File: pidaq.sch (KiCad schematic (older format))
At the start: 7 parts, among them J5 Conn_01x03_Male, J6 Conn_01x08_Female, U3 SN74LV1T34DCKR

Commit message: completed design 2.0
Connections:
- net GND: now also J6.5 (Pin_5); no longer J6.4 (Pin_4)
- net IRQ: now also J6.4 (Pin_4); no longer J6.3 (Pin_3)
- net MISO_SAFE: now also J6.8 (Pin_8); no longer J6.7 (Pin_7)
- net MOSI: now also J6.6 (Pin_6); no longer J6.5 (Pin_5)
- net SCLK: now also J6.7 (Pin_7); no longer J6.6 (Pin_6)
- net ~RST: now also J6.3 (Pin_3); no longer J6.2 (Pin_2)
- net ~SEN: now also J6.1 (Pin_1); no longer J6.8 (Pin_8)
- net ~TC: now also J6.2 (Pin_2); no longer J6.1 (Pin_1)
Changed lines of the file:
@@
 	1    0    0    -1
 $EndComp
-Text GLabel 9150 2900 0    50   Input ~ 0
+Text GLabel 9150 2200 0    50   Input ~ 0
 ~SEN
-Text GLabel 9150 2400 0    50   Input ~ 0
+Text GLabel 9150 2500 0    50   Input ~ 0
 IRQ
-Text GLabel 9150 2500 0    50   Input ~ 0
+Text GLabel 9150 2600 0    50   Input ~ 0
 GND
+Text GLabel 9150 2800 0    50   Input ~ 0
+SCLK
 Text GLabel 9150 2700 0    50   Input ~ 0
-SCLK
-Text GLabel 9150 2600 0    50   Input ~ 0
 MOSI
 Text GLabel 6750 2850 0    50   Input ~ 0
@@
 GND
 Wire Wire Line
-	9150 2800 8250 2800
-Wire Wire Line
 	8250 2800 8250 2850
 Wire Notes Line
@@
 Text Label 8350 2800 0    50   ~ 0
 MISO_SAFE
-Text GLabel 9150 2200 0    50   Input ~ 0
+Text GLabel 9150 2300 0    50   Input ~ 0
 ~TC
 $Comp
@@
 Text GLabel 4600 4850 2    50   Input ~ 0
 ~RST
-Text GLabel 9150 2300 0    50   Input ~ 0
+Text GLabel 9150 2400 0    50   Input ~ 0
 ~RST
+Wire Wire Line
+	8250 2800 8800 2800
+Wire Wire Line
+	8800 2800 8800 2900
+Wire Wire Line
+	8800 2900 9150 2900
 $EndSCHEMATC

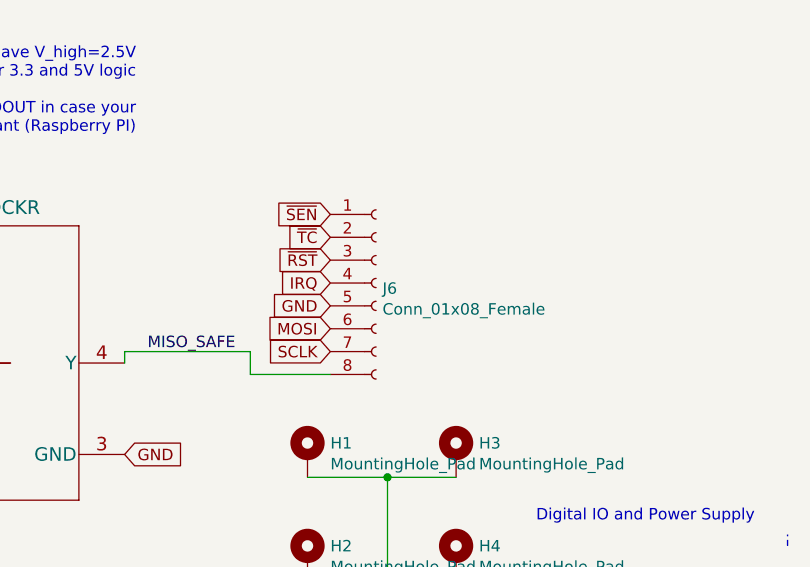
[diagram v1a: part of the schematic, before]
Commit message: pcb size reduced to 3x3in
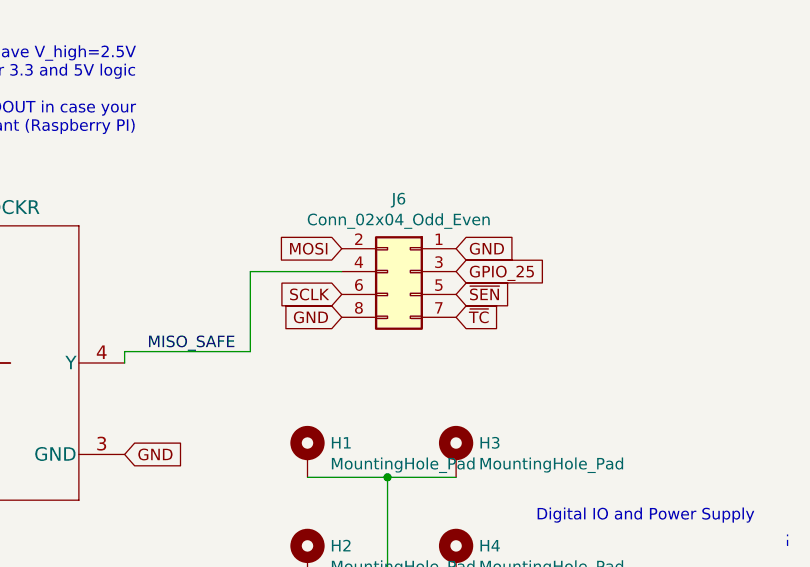
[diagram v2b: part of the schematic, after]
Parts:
- removed J6: Conn_01x08_Female, Connector_PinHeader_2.54mm:PinHeader_1x08_P2.54mm_Vertical, symbol Connector:Conn_01x08_Female
- added J6: Conn_02x04_Odd_Even, Connector_PinSocket_2.54mm:PinSocket_2x04_P2.54mm_Vertical, symbol Connector_Generic:Conn_02x04_Odd_Even
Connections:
- net GND: now also J6.1 (Pin_1), J6.8 (Pin_8)
- net MISO_SAFE: now also J6.4 (Pin_4)
- net MOSI: now also J6.2 (Pin_2)
- net SCLK: now also J6.6 (Pin_6)
- net ~SEN: now also J6.5 (Pin_5)
- net ~TC: now also J6.7 (Pin_7)
- new net GPIO_25: J6.3 (Pin_3)
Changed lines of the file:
@@
 	1250 2100 1250 2150
 Connection ~ 1250 2150
-$Comp
-L Connector:Conn_01x08_Female J6
-U 1 1 5F088E4C
-P 9350 2500
-F 0 "J6" H 9378 2476 50  0000 L CNN
-F 1 "Conn_01x08_Female" H 9378 2385 50  0000 L CNN
-F 2 "Connector_PinHeader_2.54mm:PinHeader_1x08_P2.54mm_Vertical" H 9350 2500 50  0001 C CNN
-F 3 "~" H 9350 2500 50  0001 C CNN
-	1    9350 2500
-	1    0    0    -1
-$EndComp
-Text GLabel 9150 2200 0    50   Input ~ 0
-~SEN
-Text GLabel 9150 2500 0    50   Input ~ 0
-IRQ
-Text GLabel 9150 2600 0    50   Input ~ 0
-GND
-Text GLabel 9150 2800 0    50   Input ~ 0
-SCLK
-Text GLabel 9150 2700 0    50   Input ~ 0
-MOSI
 Text GLabel 6750 2850 0    50   Input ~ 0
 MISO
@@
 Text Label 8350 2800 0    50   ~ 0
 MISO_SAFE
-Text GLabel 9150 2300 0    50   Input ~ 0
-~TC
 $Comp
 L Mechanical:MountingHole_Pad H1
@@
 Text GLabel 4600 4850 2    50   Input ~ 0
 ~RST
-Text GLabel 9150 2400 0    50   Input ~ 0
-~RST
 Wire Wire Line
 	8250 2800 8800 2800
+Text GLabel 9200 2350 0    50   Input ~ 0
+MOSI
+Text GLabel 9200 2550 0    50   Input ~ 0
+SCLK
+Text GLabel 9200 2650 0    50   Input ~ 0
+GND
+Text GLabel 9700 2650 2    50   Input ~ 0
+~TC
+Text GLabel 9700 2550 2    50   Input ~ 0
+~SEN
+Text GLabel 9700 2450 2    50   Input ~ 0
+GPIO_25
+Text GLabel 9700 2350 2    50   Input ~ 0
+GND
 Wire Wire Line
-	8800 2800 8800 2900
+	8800 2800 8800 2450
+$Comp
+L Connector_Generic:Conn_02x04_Odd_Even J6
+U 1 1 5EE81435
+P 9500 2450
+F 0 "J6" H 9550 2767 50  0000 C CNN
+F 1 "Conn_02x04_Odd_Even" H 9550 2676 50  0000 C CNN
+F 2 "Connector_PinSocket_2.54mm:PinSocket_2x04_P2.54mm_Vertical" H 9500 2450 50  0001 C CNN
+F 3 "~" H 9500 2450 50  0001 C CNN
+	1    9500 2450
+	-1   0    0    -1
+$EndComp
 Wire Wire Line
-	8800 2900 9150 2900
+	8800 2450 9200 2450
 $EndSCHEMATC
